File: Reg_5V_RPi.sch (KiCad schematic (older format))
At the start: 13 parts, among them U20 TPS54340

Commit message: changed L and D of RPi 5V reg, all components on one side, everything routed, silkscreen unfinished
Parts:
- D20: footprint hedgehog_footprints:SMC -> hedgehog_footprints:PDS760-13
- L20: footprint hedgehog_footprints:VLP8040 -> hedgehog_footprints:XAL4030
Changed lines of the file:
@@
 F 0 "L20" V 6975 3325 50  0000 C CNN
 F 1 "4µ7" V 6900 3325 50  0000 C CNN
-F 2 "hedgehog_footprints:VLP8040" H 6825 3325 50  0001 C CNN
+F 2 "hedgehog_footprints:XAL4030" H 6825 3325 50  0001 C CNN
 F 3 "" H 6825 3325 50  0001 C CNN
 	1    6825 3325
@@
 F 0 "D20" V 6529 3518 50  0000 L CNN
 F 1 "D" V 6620 3518 50  0000 L CNN
-F 2 "hedgehog_footprints:SMC" V 6575 3450 50  0001 C CNN
+F 2 "hedgehog_footprints:PDS760-13" V 6575 3450 50  0001 C CNN
 F 3 "" V 6575 3450 50  0001 C CNN
 	1    6575 3450

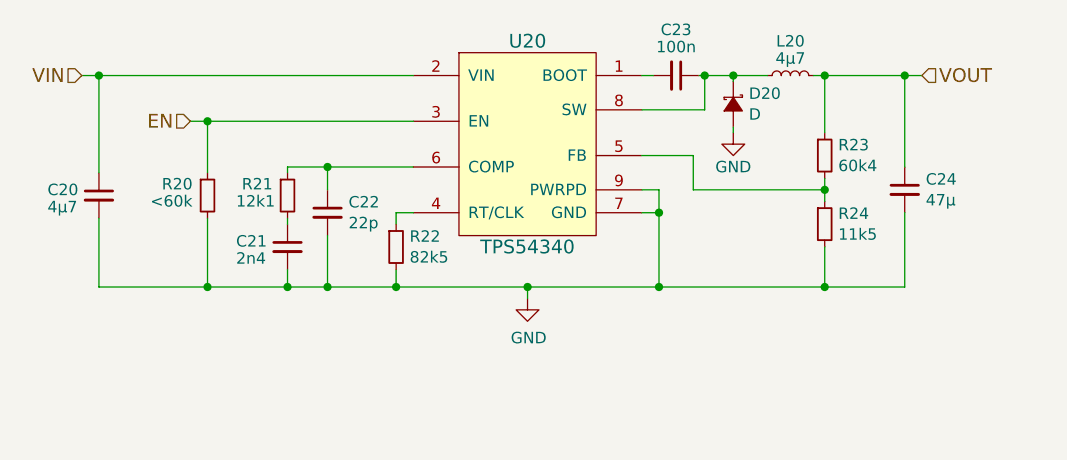
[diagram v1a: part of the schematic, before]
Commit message: lots of changes: - incremented version number to 0.2 - all inputs are now analog, vbat for supply voltage monitoring - 6 servos - different 5v 10A regulator - changed input order - footprint fixes and cosmetic hanges - added fiducials - board size 0.5mm smaller - lots of other fixes and small changes
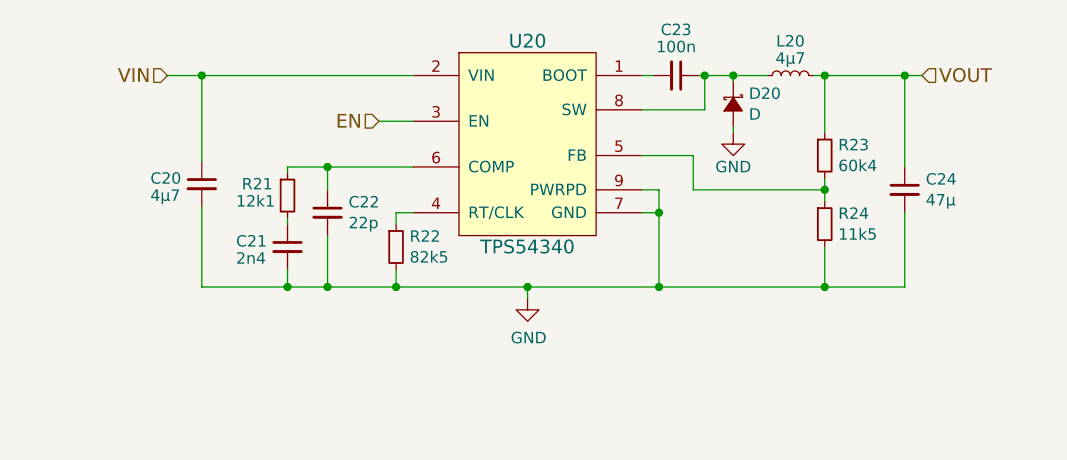
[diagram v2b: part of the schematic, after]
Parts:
- removed R20: <60k, Resistors_SMD:R_0603, symbol R_Small
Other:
- moved on the sheet: C20
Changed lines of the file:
@@
-EESchema Schematic File Version 2
+EESchema Schematic File Version 3
 LIBS:power
 LIBS:device
-LIBS:transistors
-LIBS:conn
 LIBS:linear
 LIBS:regul
-LIBS:74xx
-LIBS:cmos4000
 LIBS:adc-dac
 LIBS:memory
@@
 LIBS:digital-audio
 LIBS:philips
-LIBS:display
 LIBS:cypress
 LIBS:siliconi
@@
 LIBS:atmel
 LIBS:contrib
-LIBS:valves
 LIBS:hedgehog_symbols
-LIBS:switches
 LIBS:Hedgehog-cache
 EELAYER 26 0
@@
 Comment4 ""
 $EndDescr
-Text HLabel 3725 3325 0    60   Input ~ 0
+Text HLabel 4100 3325 0    60   Input ~ 0
 VIN
-Text HLabel 4200 3525 0    60   Input ~ 0
+Text HLabel 5025 3525 0    60   Input ~ 0
 EN
 Text HLabel 7400 3325 2    60   Input ~ 0
@@
 L C_Small C20
 U 1 1 590647C4
-P 3800 3850
-F 0 "C20" H 3575 3875 50  0000 L CNN
-F 1 "4µ7" H 3575 3800 50  0000 L CNN
-F 2 "Capacitors_SMD:C_0603" H 3800 3850 50  0001 C CNN
-F 3 "" H 3800 3850 50  0001 C CNN
-	1    3800 3850
+P 4250 3800
+F 0 "C20" H 4025 3825 50  0000 L CNN
+F 1 "4µ7" H 4025 3750 50  0000 L CNN
+F 2 "Capacitors_SMD:C_0603" H 4250 3800 50  0001 C CNN
+F 3 "" H 4250 3800 50  0001 C CNN
+	1    4250 3800
 	1    0    0    -1
 $EndComp
@@
 	0    1    1    0
 $EndComp
-$Comp
-L R_Small R20
-U 1 1 590652CD
-P 4275 3850
-F 0 "R20" H 4075 3900 50  0000 L CNN
-F 1 "<60k" H 4025 3825 50  0000 L CNN
-F 2 "Resistors_SMD:R_0603" H 4275 3850 50  0001 C CNN
-F 3 "" H 4275 3850 50  0001 C CNN
-	1    4275 3850
-	1    0    0    -1
-$EndComp
 Wire Wire Line
 	5175 3925 5100 3925
@@
 Connection ~ 4800 3725
 Wire Wire Line
-	4200 3525 5175 3525
-Wire Wire Line
-	4275 3750 4275 3525
-Connection ~ 4275 3525
-Wire Wire Line
-	3725 3325 5175 3325
-Wire Wire Line
-	3800 3325 3800 3750
-Connection ~ 3800 3325
+	5025 3525 5175 3525
+Wire Wire Line
+	4100 3325 5175 3325
+Wire Wire Line
+	4250 3325 4250 3700
+Connection ~ 4250 3325
 Wire Wire Line
 	6175 3325 6225 3325
@@
 Connection ~ 6975 3825
 Wire Wire Line
-	3800 4250 7325 4250
-Wire Wire Line
-	3800 4250 3800 3950
-Wire Wire Line
-	4275 3950 4275 4250
-Connection ~ 4275 4250
+	4250 4250 7325 4250
+Wire Wire Line
+	4250 4250 4250 3900
 Wire Wire Line
 	4625 4175 4625 4250

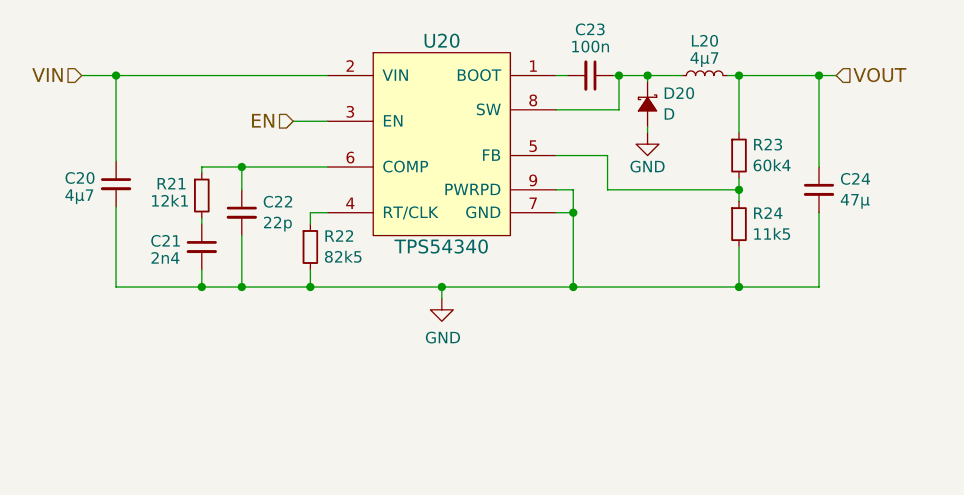
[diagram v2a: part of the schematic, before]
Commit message: component values changed documentation added
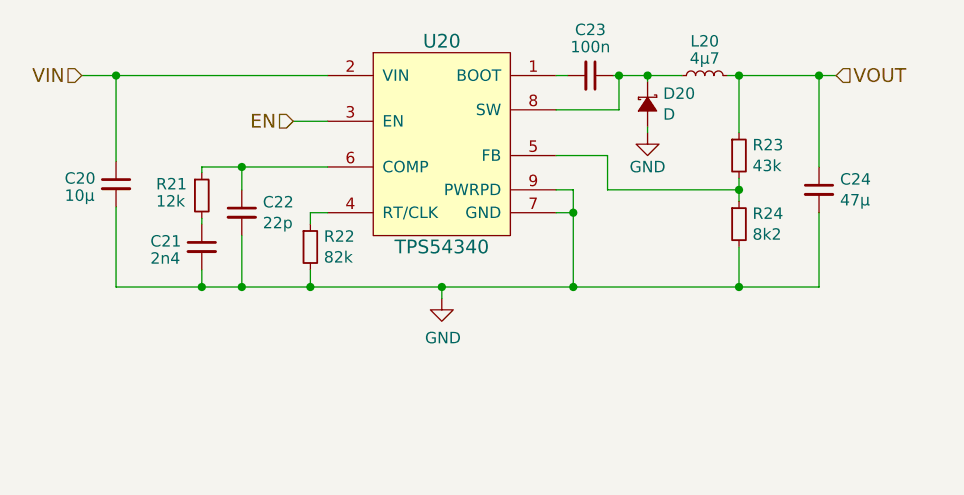
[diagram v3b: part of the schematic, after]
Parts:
- C20: value 4µ7 -> 10µ
- R21: value 12k1 -> 12k
- R22: value 82k5 -> 82k
- R23: value 60k4 -> 43k
- R24: value 11k5 -> 8k2
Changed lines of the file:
@@
 P 4250 3800
 F 0 "C20" H 4025 3825 50  0000 L CNN
-F 1 "4µ7" H 4025 3750 50  0000 L CNN
+F 1 "10µ" H 4025 3750 50  0000 L CNN
 F 2 "Capacitors_SMD:C_0603" H 4250 3800 50  0001 C CNN
 F 3 "" H 4250 3800 50  0001 C CNN
@@
 P 4625 3850
 F 0 "R21" H 4425 3900 50  0000 L CNN
-F 1 "12k1" H 4400 3825 50  0000 L CNN
+F 1 "12k" H 4425 3825 50  0000 L CNN
 F 2 "Resistors_SMD:R_0603" H 4625 3850 50  0001 C CNN
 F 3 "" H 4625 3850 50  0001 C CNN
@@
 P 5100 4075
 F 0 "R22" H 5159 4121 50  0000 L CNN
-F 1 "82k5" H 5159 4030 50  0000 L CNN
+F 1 "82k" H 5159 4030 50  0000 L CNN
 F 2 "Resistors_SMD:R_0603" H 5100 4075 50  0001 C CNN
 F 3 "" H 5100 4075 50  0001 C CNN
@@
 P 6975 3675
 F 0 "R23" H 7034 3721 50  0000 L CNN
-F 1 "60k4" H 7034 3630 50  0000 L CNN
+F 1 "43k" H 7034 3630 50  0000 L CNN
 F 2 "Resistors_SMD:R_0603" H 6975 3675 50  0001 C CNN
 F 3 "" H 6975 3675 50  0001 C CNN
@@
 P 6975 3975
 F 0 "R24" H 7034 4021 50  0000 L CNN
-F 1 "11k5" H 7034 3930 50  0000 L CNN
+F 1 "8k2" H 7034 3930 50  0000 L CNN
 F 2 "Resistors_SMD:R_0603" H 6975 3975 50  0001 C CNN
 F 3 "" H 6975 3975 50  0001 C CNN

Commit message: upgraded project to new kicad symbol library format
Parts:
- C20, C21, C22, C23, C24: symbol C_Small -> Device:C_Small
- D20: symbol D_Schottky_Small_ALT -> Device:D_Schottky_Small_ALT
- L20: symbol L_Small -> Device:L_Small
- R21, R22, R23, R24: symbol R_Small -> Device:R_Small
- U20: symbol TPS54340 -> hedgehog_symbols:TPS54340
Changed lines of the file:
@@
-EESchema Schematic File Version 3
-LIBS:power
-LIBS:device
-LIBS:linear
-LIBS:regul
-LIBS:adc-dac
-LIBS:memory
-LIBS:xilinx
-LIBS:microcontrollers
-LIBS:dsp
-LIBS:microchip
-LIBS:analog_switches
-LIBS:motorola
-LIBS:texas
-LIBS:intel
-LIBS:audio
-LIBS:interface
-LIBS:digital-audio
-LIBS:philips
-LIBS:cypress
-LIBS:siliconi
-LIBS:opto
-LIBS:atmel
-LIBS:contrib
-LIBS:hedgehog_symbols
-LIBS:ac-dc
-LIBS:Altera
-LIBS:analog_devices
-LIBS:Battery_Management
-LIBS:bbd
-LIBS:bosch
-LIBS:brooktre
-LIBS:Connector
-LIBS:dc-dc
-LIBS:Diode
-LIBS:Display
-LIBS:driver_gate
-LIBS:DSP_Microchip_DSPIC33
-LIBS:elec-unifil
-LIBS:ESD_Protection
-LIBS:Espressif
-LIBS:FPGA_Actel
-LIBS:ftdi
-LIBS:gennum
-LIBS:Graphic
-LIBS:hc11
-LIBS:infineon
-LIBS:intersil
-LIBS:ir
-LIBS:Lattice
-LIBS:LED
-LIBS:LEM
-LIBS:Logic_74xgxx
-LIBS:Logic_74xx
-LIBS:Logic_CMOS_4000
-LIBS:Logic_CMOS_IEEE
-LIBS:logic_programmable
-LIBS:Logic_TTL_IEEE
-LIBS:maxim
-LIBS:MCU_Microchip_PIC10
-LIBS:MCU_Microchip_PIC12
-LIBS:MCU_Microchip_PIC16
-LIBS:MCU_Microchip_PIC18
-LIBS:MCU_Microchip_PIC24
-LIBS:MCU_Microchip_PIC32
-LIBS:MCU_NXP_Kinetis
-LIBS:MCU_NXP_LPC
-LIBS:MCU_NXP_S08
-LIBS:MCU_ST_STM8
-LIBS:MCU_Texas_MSP430
-LIBS:Mechanical
-LIBS:modules
-LIBS:Motor
-LIBS:motor_drivers
-LIBS:nordicsemi
-LIBS:nxp
-LIBS:onsemi
-LIBS:Oscillators
-LIBS:powerint
-LIBS:Power_Management
-LIBS:pspice
-LIBS:references
-LIBS:Relay
-LIBS:rfcom
-LIBS:RFSolutions
-LIBS:Sensor_Current
-LIBS:sensors
-LIBS:silabs
-LIBS:supertex
-LIBS:Switch
-LIBS:Transformer
-LIBS:Transistor
-LIBS:triac_thyristor
-LIBS:Valve
-LIBS:video
-LIBS:wiznet
-LIBS:Worldsemi
-LIBS:Xicor
-LIBS:zetex
-LIBS:Zilog
-LIBS:Hedgehog-cache
+EESchema Schematic File Version 4
 EELAYER 26 0
 EELAYER END
@@
 VOUT
 $Comp
-L TPS54340 U20
+L hedgehog_symbols:TPS54340 U20
 U 1 1 590645FD
 P 5675 3625
@@
 $EndComp
 $Comp
-L C_Small C20
+L Device:C_Small C20
 U 1 1 590647C4
 P 4250 3800
@@
 $EndComp
 $Comp
-L C_Small C21
+L Device:C_Small C21
 U 1 1 59064874
 P 4625 4075
@@
 $EndComp
 $Comp
-L C_Small C22
+L Device:C_Small C22
 U 1 1 590648E6
 P 4800 3925
@@
 $EndComp
 $Comp
-L C_Small C23
+L Device:C_Small C23
 U 1 1 59064924
 P 6325 3325
@@
 $EndComp
 $Comp
-L C_Small C24
+L Device:C_Small C24
 U 1 1 59064990
 P 7325 3825
@@
 $EndComp
 $Comp
-L R_Small R21
+L Device:R_Small R21
 U 1 1 59064A14
 P 4625 3850
@@
 $EndComp
 $Comp
-L R_Small R22
+L Device:R_Small R22
 U 1 1 59064AB0
 P 5100 4075
@@
 $EndComp
 $Comp
-L R_Small R23
+L Device:R_Small R23
 U 1 1 59064B04
 P 6975 3675
@@
 $EndComp
 $Comp
-L R_Small R24
+L Device:R_Small R24
 U 1 1 59064B72
 P 6975 3975
@@
 $EndComp
 $Comp
-L L_Small L20
+L Device:L_Small L20
 U 1 1 59064BF4
 P 6825 3325
@@
 $EndComp
 $Comp
-L D_Schottky_Small_ALT D20
+L Device:D_Schottky_Small_ALT D20
 U 1 1 59064D44
 P 6575 3450
@@
 	6975 3775 6975 3875
 $Comp
-L GND #PWR07
+L power:GND #PWR07
 U 1 1 59066211
 P 5675 4300
@@
 $EndComp
 $Comp
-L GND #PWR08
+L power:GND #PWR08
 U 1 1 5906623D
 P 6575 3575
